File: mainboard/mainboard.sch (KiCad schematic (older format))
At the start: 116 parts, among them J1 USB_B_Micro, J2 Conn_01x02_MountingPin, J3 Conn_01x19_MountingPin, J4 Conn_01x19_MountingPin, Q1 DMG2301L, Q2 MMBT3904, Q3 MMBT3904, SW1 SW_Push, SW2 SW_Push, U1 tps63070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

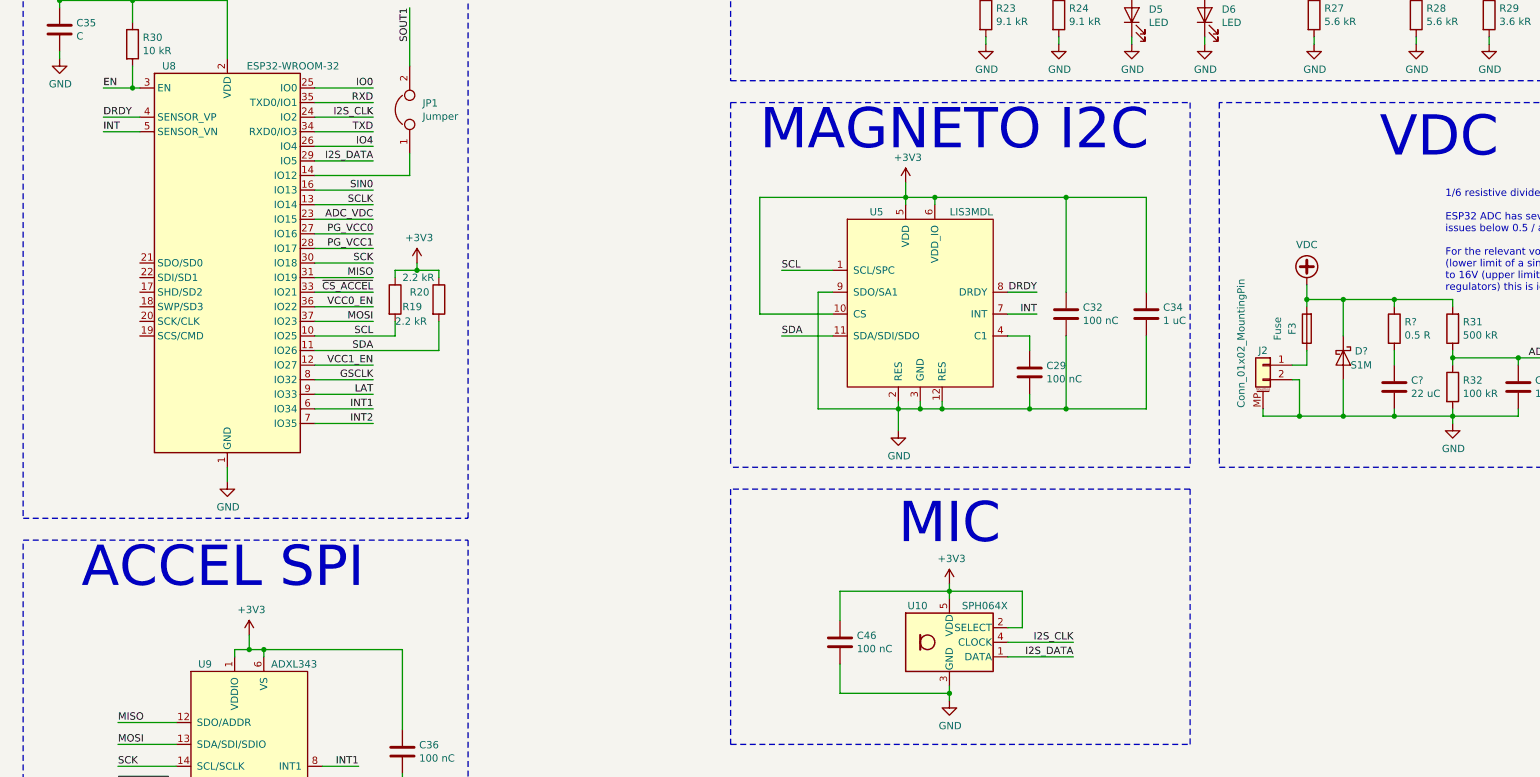
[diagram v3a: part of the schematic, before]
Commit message: Replace magnetometer by MC6470
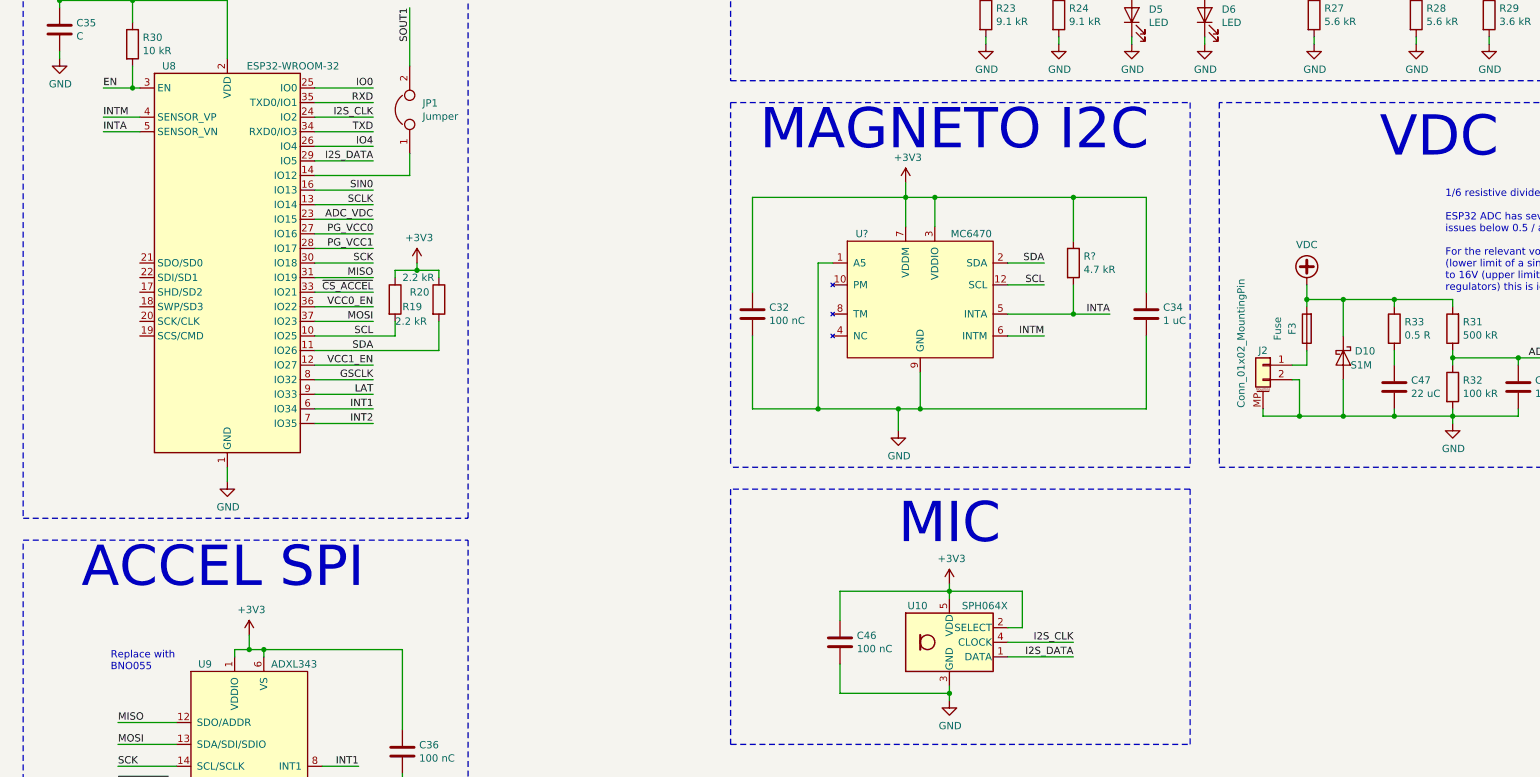
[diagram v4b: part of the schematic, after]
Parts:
- removed C29: 100 nC, Capacitor_SMD:C_0805_2012Metric, symbol Device:C
- removed U5: LIS3MDL, Package_LGA:LGA-12_2x2mm_P0.5mm, symbol LIS3MDL:LIS3MDL
- added R?: 4.7 kR, Resistor_SMD:R_0805_2012Metric, symbol Device:R
- added U?: MC6470, Package_LGA:LGA-12_2x2mm_P0.5mm, symbol MC6470:MC6470
- gave numbers to parts that had none: 3
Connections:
- net +3V3: now also R?.1, U?.3 (VDDIO), U?.7 (VDDM)
- net GND: now also U?.1 (A5), U?.9 (GND)
- net SCL: now also U?.12 (SCL)
- net SDA: now also U?.2 (SDA)
- net DRDY renamed INTM
- net INTM: now also U?.6 (INTM)
- net INT renamed INTA
- net INTA: now also R?.2, U?.5 (INTA)
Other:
- note added: "Replace with\nBNO055"
- moved on the sheet: C32
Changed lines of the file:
@@
 Text Notes 10600 8800 0    276  ~ 0
 ACCEL SPI
-$Comp
-L LIS3MDL:LIS3MDL U5
-U 1 1 5CFD8A1C
-P 16350 6800
-F 0 "U5" H 16050 7400 50  0000 C CNN
-F 1 "LIS3MDL" H 16700 7400 50  0000 C CNN
-F 2 "Package_LGA:LGA-12_2x2mm_P0.5mm" H 16350 6800 50  0001 C CNN
-F 3 "" H 16350 6800 50  0001 C CNN
-	1    16350 6800
-	1    0    0    -1
-$EndComp
 Wire Notes Line
 	15050 5450 18200 5450
@@
 L Device:C C32
 U 1 1 5D017696
-P 17350 6900
-F 0 "C32" H 17465 6946 50  0000 L CNN
-F 1 "100 nC" H 17465 6855 50  0000 L CNN
-F 2 "Capacitor_SMD:C_0805_2012Metric" H 17388 6750 50  0001 C CNN
-F 3 "~" H 17350 6900 50  0001 C CNN
-	1    17350 6900
-	1    0    0    -1
-$EndComp
-Wire Wire Line
-	16250 6150 16250 6100
+P 15200 6900
+F 0 "C32" H 15315 6946 50  0000 L CNN
+F 1 "100 nC" H 15315 6855 50  0000 L CNN
+F 2 "Capacitor_SMD:C_0805_2012Metric" H 15238 6750 50  0001 C CNN
+F 3 "~" H 15200 6900 50  0001 C CNN
+	1    15200 6900
+	1    0    0    -1
+$EndComp
 Wire Wire Line
 	16250 6100 16450 6100
-Wire Wire Line
-	16450 6100 16450 6150
-Wire Wire Line
-	16450 6100 17350 6100
-Wire Wire Line
-	17350 6100 17350 6750
 Connection ~ 16450 6100
 Wire Wire Line
-	16350 7500 16350 7550
-Wire Wire Line
-	16350 7550 16500 7550
-Wire Wire Line
-	16500 7550 16500 7500
-Wire Wire Line
 	16350 7550 16200 7550
-Wire Wire Line
-	16200 7550 16200 7500
 Connection ~ 16350 7550
-Wire Wire Line
-	16500 7550 17100 7550
-Wire Wire Line
-	17350 7550 17350 7050
-Connection ~ 16500 7550
 $Comp
 L power:+3V3 #PWR017
@@
 Text Label 12600 6950 2    50   ~ 0
 MOSI
-$Comp
-L Device:C C29
-U 1 1 5D1A98CC
-P 17100 7300
-F 0 "C29" H 17215 7346 50  0000 L CNN
-F 1 "100 nC" H 17215 7255 50  0000 L CNN
-F 2 "Capacitor_SMD:C_0805_2012Metric" H 17138 7150 50  0001 C CNN
-F 3 "~" H 17100 7300 50  0001 C CNN
-	1    17100 7300
-	1    0    0    -1
-$EndComp
-Wire Wire Line
-	17100 7450 17100 7550
-Connection ~ 17100 7550
-Wire Wire Line
-	17100 7550 17350 7550
-Wire Wire Line
-	16950 7050 17100 7050
-Wire Wire Line
-	17100 7050 17100 7150
-Wire Wire Line
-	15750 6900 15250 6900
-Wire Wire Line
-	15250 6900 15250 6100
-Wire Wire Line
-	15250 6100 16250 6100
-Wire Wire Line
-	15750 6600 15400 6600
-Wire Wire Line
-	15750 7050 15400 7050
-Text Label 15400 6600 0    50   ~ 0
+Text Label 17200 6700 2    50   ~ 0
 SCL
-Text Label 15400 7050 0    50   ~ 0
+Text Label 17200 6550 2    50   ~ 0
 SDA
 Text Label 10850 9850 0    50   ~ 0
@@
 Text Label 12500 10150 2    50   ~ 0
 INT2
-Wire Wire Line
-	16950 6750 17150 6750
-Wire Wire Line
-	16950 6900 17150 6900
-Text Label 17150 6750 2    50   ~ 0
-DRDY
-Text Label 17150 6900 2    50   ~ 0
-INT
+Text Label 17200 7050 2    50   ~ 0
+INTM
+Text Label 17650 6900 2    50   ~ 0
+INTA
 Wire Wire Line
 	11000 5550 10750 5550
@@
 	11000 5650 10750 5650
 Text Label 10750 5550 0    50   ~ 0
-DRDY
+INTM
 Text Label 10750 5650 0    50   ~ 0
-INT
+INTA
 $Comp
 L Device:Jumper JP1
@@
 	8700 9500 8800 9500
 Wire Wire Line
-	15750 6750 15650 6750
-Wire Wire Line
-	15650 6750 15650 7550
-Wire Wire Line
 	15650 7550 16200 7550
 $Comp
@@
 	17900 7050 17900 7550
 Wire Wire Line
-	17900 7550 17350 7550
-Connection ~ 17350 7550
-Wire Wire Line
 	17900 6750 17900 6100
-Wire Wire Line
-	17900 6100 17350 6100
-Connection ~ 17350 6100
 Wire Wire Line
 	8800 9500 8800 9100
@@
 Connection ~ 18950 7600
 $Comp
-L Device:R R?
+L Device:R R33
 U 1 1 5E9DA20F
 P 19600 7000
-F 0 "R?" H 19670 7046 50  0000 L CNN
+F 0 "R33" H 19670 7046 50  0000 L CNN
 F 1 "0.5 R" H 19670 6955 50  0000 L CNN
 F 2 "Resistor_SMD:R_1210_3225Metric" V 19530 7000 50  0001 C CNN
@@
 $EndComp
 $Comp
-L Device:C C?
+L Device:C C47
 U 1 1 5EA32808
 P 19600 7400
-F 0 "C?" H 19715 7446 50  0000 L CNN
+F 0 "C47" H 19715 7446 50  0000 L CNN
 F 1 "22 uC" H 19715 7355 50  0000 L CNN
 F 2 "Capacitor_SMD:C_1210_3225Metric" H 19638 7250 50  0001 C CNN
@@
 	19600 7600 20000 7600
 $Comp
-L Device:D_Schottky D?
+L Device:D_Schottky D10
 U 1 1 5EC98730
 P 19250 7200
-F 0 "D?" V 19204 7279 50  0000 L CNN
+F 0 "D10" V 19204 7279 50  0000 L CNN
 F 1 "S1M" V 19300 7250 50  0000 L CNN
 F 2 "Diode_SMD:D_SMA" H 19250 7200 50  0001 C CNN
@@
 Wire Wire Line
 	19250 7350 19250 7600
+Text Notes 10800 9350 0    50   ~ 0
+Replace with\nBNO055
+$Comp
+L MC6470:MC6470 U?
+U 1 1 5EDD55F4
+P 16350 6800
+F 0 "U?" H 15950 7250 50  0000 C CNN
+F 1 "MC6470" H 16700 7250 50  0000 C CNN
+F 2 "Package_LGA:LGA-12_2x2mm_P0.5mm" H 16350 6850 50  0001 C CNN
+F 3 "" H 16350 6850 50  0001 C CNN
+	1    16350 6800
+	1    0    0    -1
+$EndComp
+Wire Wire Line
+	16950 7050 17200 7050
+Wire Wire Line
+	17200 6700 16950 6700
+Wire Wire Line
+	16950 6550 17200 6550
+Wire Wire Line
+	16350 7300 16350 7550
+Wire Wire Line
+	16250 6100 16250 6300
+Wire Wire Line
+	16450 6100 16450 6300
+Wire Wire Line
+	15650 7550 15650 6550
+Wire Wire Line
+	15650 6550 15750 6550
+Wire Wire Line
+	16250 6100 15200 6100
+Wire Wire Line
+	15200 6100 15200 6750
+Wire Wire Line
+	15650 7550 15200 7550
+Wire Wire Line
+	15200 7550 15200 7050
+Connection ~ 15650 7550
+Wire Wire Line
+	16450 6100 17400 6100
+Wire Wire Line
+	16350 7550 17900 7550
+$Comp
+L Device:R R?
+U 1 1 5F2419CF
+P 17400 6550
+F 0 "R?" H 17470 6596 50  0000 L CNN
+F 1 "4.7 kR" H 17470 6505 50  0000 L CNN
+F 2 "Resistor_SMD:R_0805_2012Metric" V 17330 6550 50  0001 C CNN
+F 3 "~" H 17400 6550 50  0001 C CNN
+	1    17400 6550
+	1    0    0    -1
+$EndComp
+Wire Wire Line
+	17400 6400 17400 6100
+Connection ~ 17400 6100
+Wire Wire Line
+	17400 6100 17900 6100
+Wire Wire Line
+	17400 6700 17400 6900
+Wire Wire Line
+	16950 6900 17400 6900
+Wire Wire Line
+	17400 6900 17650 6900
 Wire Bus Line
 	8350 2150 8350 2500
 Wire Bus Line
 	9350 2500 9350 2750
+Connection ~ 17400 6900
 $EndSCHEMATC

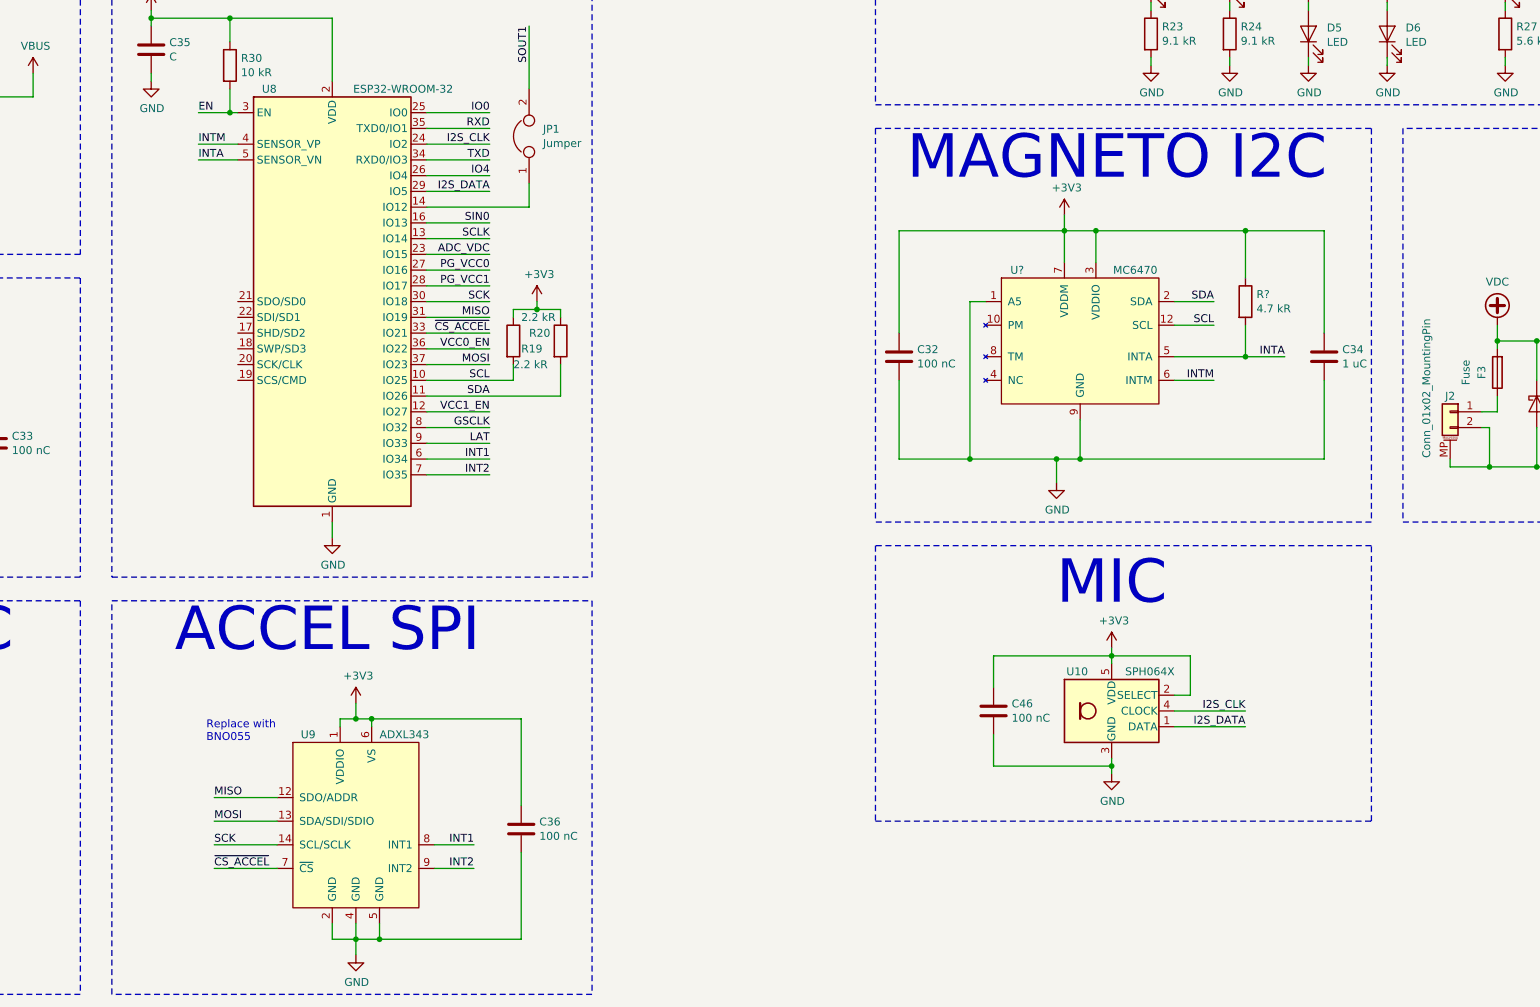
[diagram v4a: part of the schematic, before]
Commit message: Start integration of BNO055
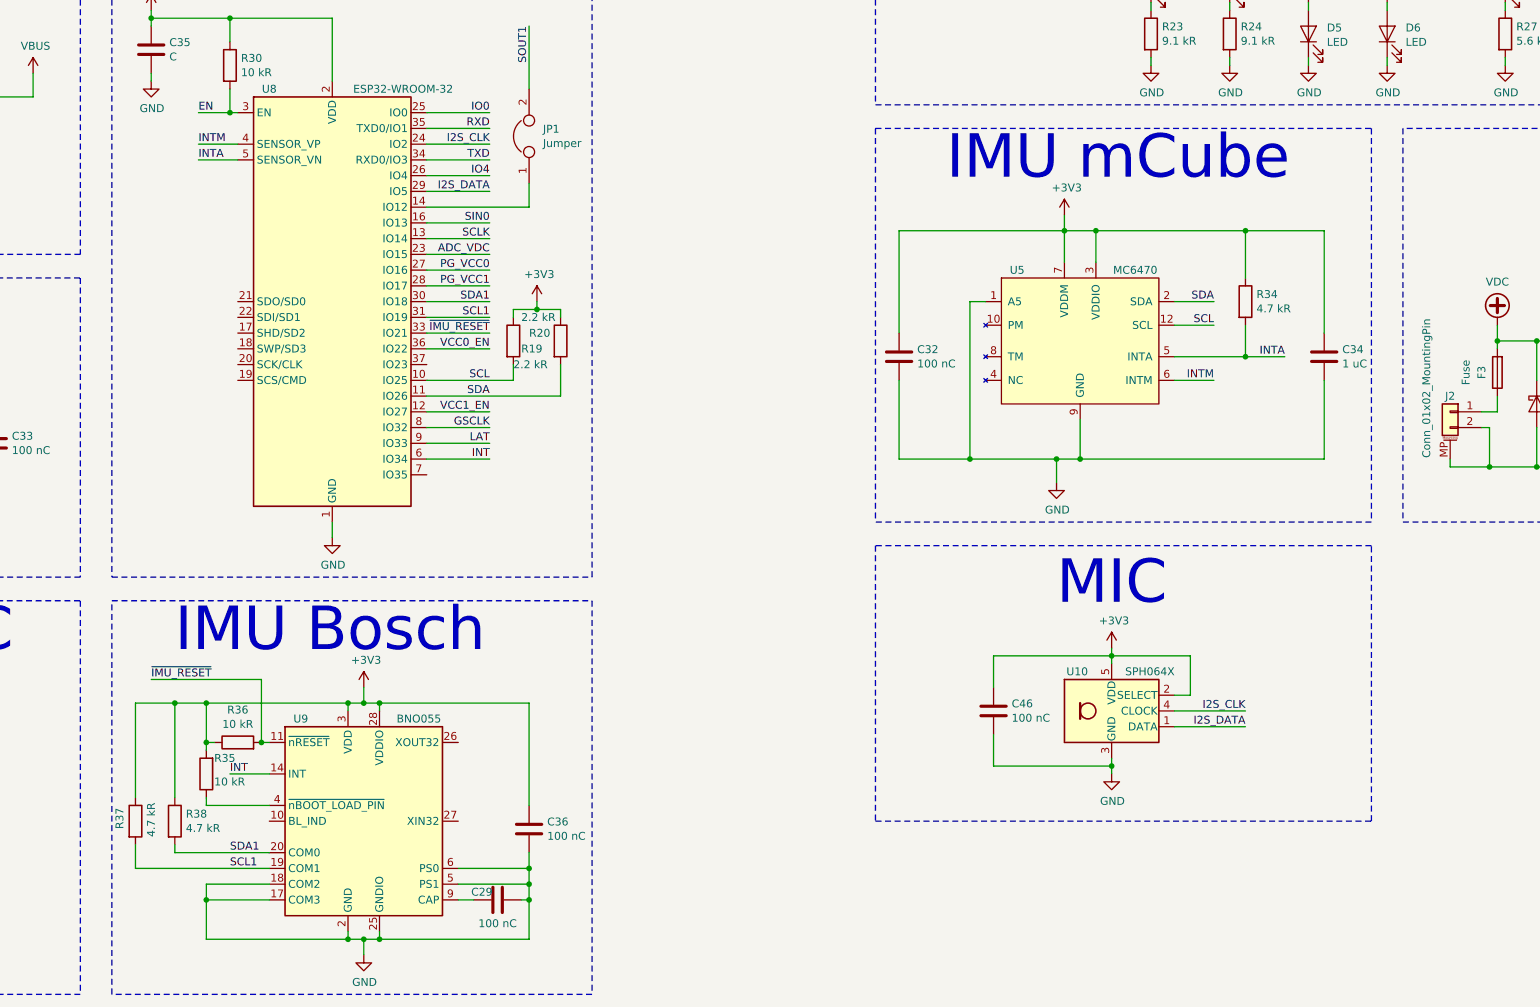
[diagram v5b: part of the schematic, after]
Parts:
- removed U9: ADXL343, Package_LGA:LGA-14_3x5mm_P0.8mm_LayoutBorder1x6y, symbol ADXL343:ADXL343
- added C29: 100 nC, Capacitor_SMD:C_0805_2012Metric, symbol Device:C
- added R35, R36: 10 kR, Resistor_SMD:R_0805_2012Metric, symbol Device:R
- added R37, R38: 4.7 kR, Resistor_SMD:R_0805_2012Metric, symbol Device:R
- added U9: BNO055, Package_LGA:LGA-28_5.2x3.8mm_P0.5mm, symbol Sensor_Motion:BNO055
- gave numbers to parts that had none: 2
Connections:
- net +3V3: now also R35.2, R36.1, R37.1, R38.1, U9.28 (VDDIO), U9.3 (VDD)
- net GND: now also C29.2, U9.15 (GNDIO), U9.16 (GNDIO), U9.17 (COM3), U9.18 (COM2), U9.2 (GND), U9.25 (GNDIO), U9.5 (PS1), U9.6 (PS0)
- net INT1 renamed INT
- net INT: now also U9.14 (INT)
- net INT2: no longer names the net of U8.7 (IO35)
- net MISO renamed SCL1
- net SCL1: now also R37.2, U9.19 (COM1)
- net MOSI: no longer names the net of U8.37 (IO23)
- net SCK renamed SDA1
- net SDA1: now also R38.2, U9.20 (COM0)
- net ~CS_ACCEL renamed ~IMU_RESET
- net ~IMU_RESET: now also R36.2, U9.11 (~nRESET)
- new net: R35.1, U9.4 (~nBOOT_LOAD_PIN)
- new net: C29.1, U9.9 (CAP)
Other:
- note added: "IMU Bosch"
- note added: "IMU mCube"
- note removed: "ACCEL SPI"
- note removed: "MAGNETO I2C"
- note removed: "Replace with\nBNO055"
- moved on the sheet: C36
